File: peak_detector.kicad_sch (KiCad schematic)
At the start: 8 parts, among them U1 AD8001AR, U2 AD8039

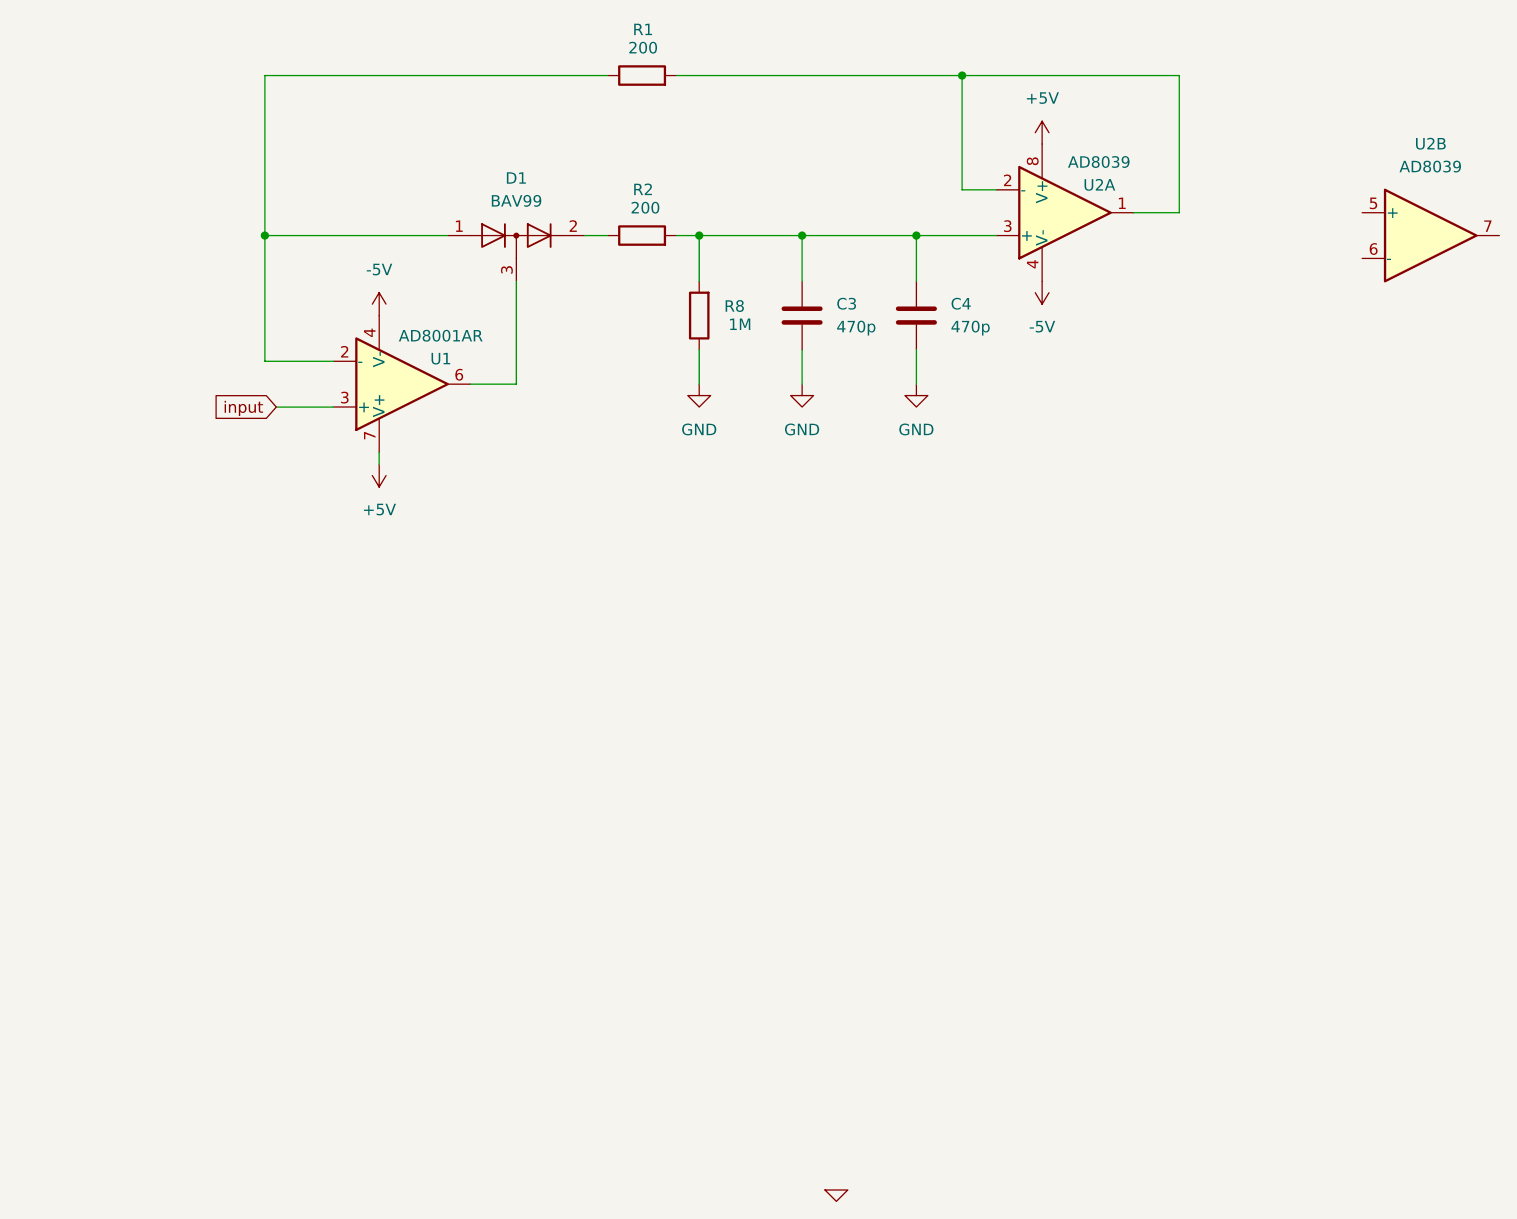
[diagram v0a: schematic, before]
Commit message: Dual bjt and MIC920.
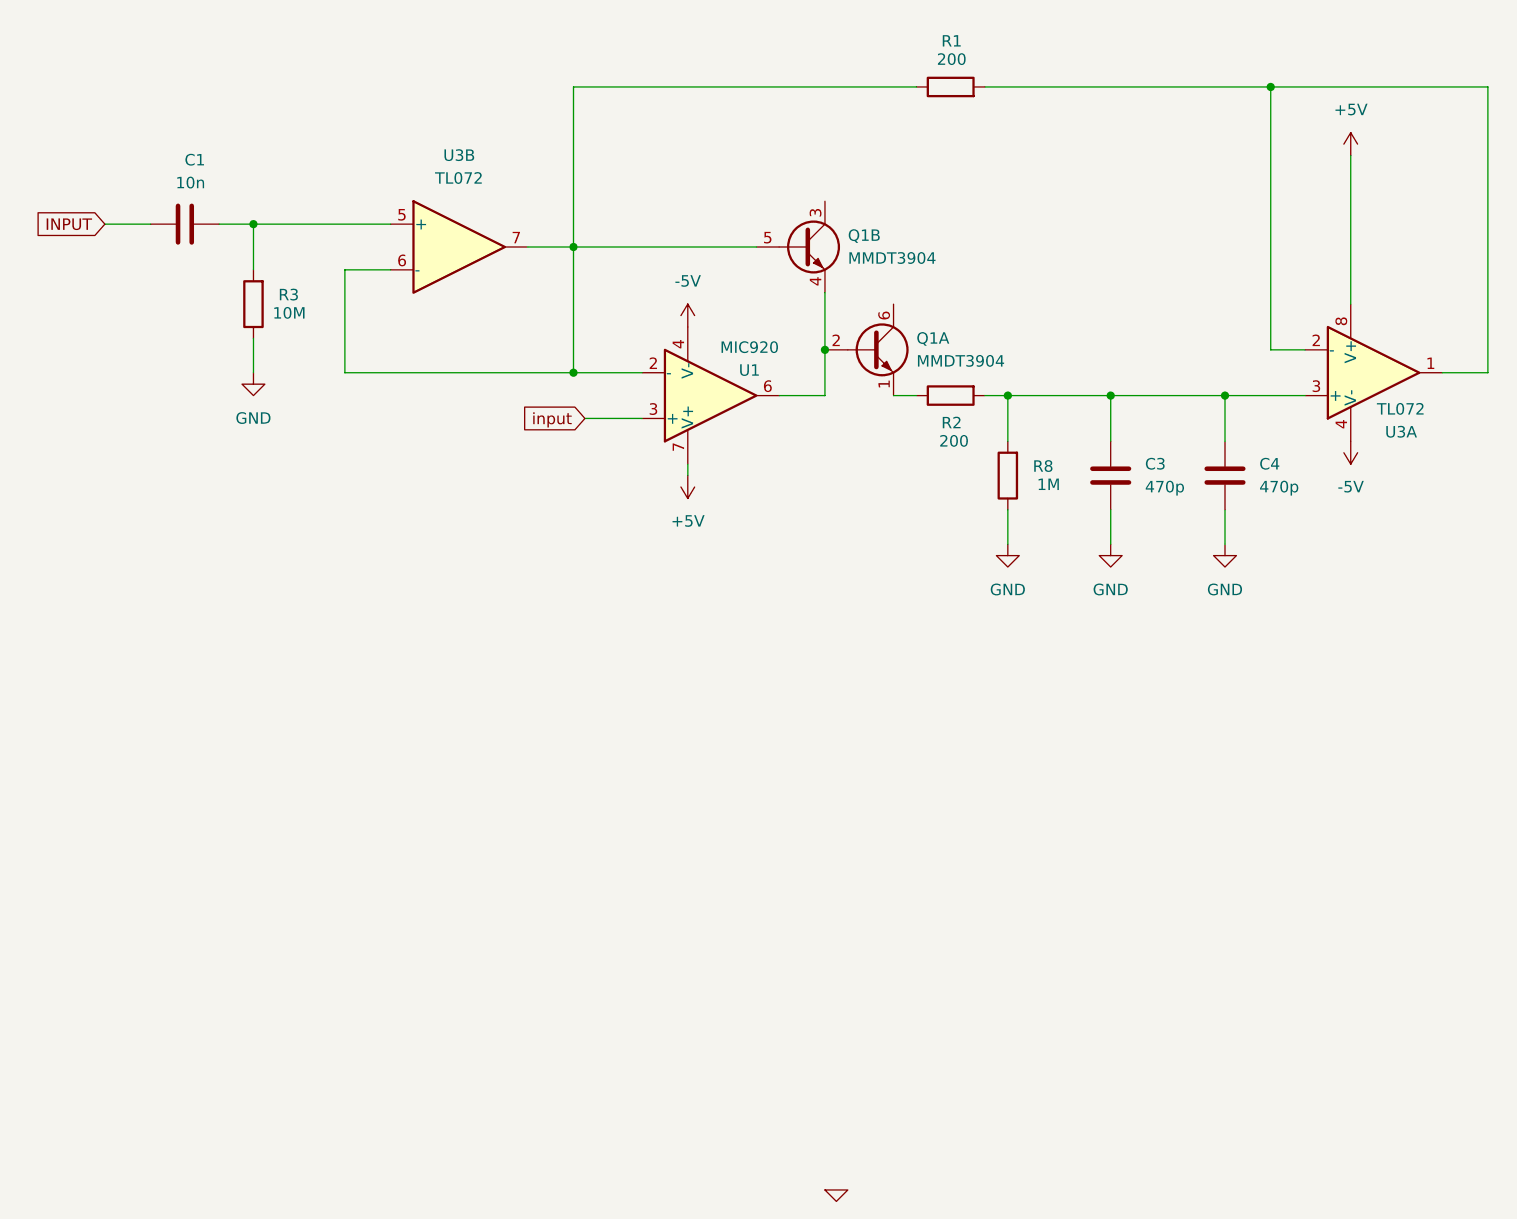
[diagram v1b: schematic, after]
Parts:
- removed D1: BAV99, Package_TO_SOT_SMD:SOT-23, symbol Diode:BAV99
- removed U2: AD8039, Package_SO:SOIC-8_3.9x4.9mm_P1.27mm, symbol Amplifier_Operational:TL072
- added C1: 10n, Capacitor_SMD:C_0603_1608Metric_Pad1.08x0.95mm_HandSolder, symbol Device:C
- added Q1: MMDT3904, Package_TO_SOT_SMD:SOT-363_SC-70-6, symbol Transistor_BJT:MMDT3904
- added R3: 10M, Resistor_SMD:R_0603_1608Metric_Pad0.98x0.95mm_HandSolder, symbol Device:R
- added U3: TL072, Package_SO:SOIC-8_3.9x4.9mm_P1.27mm, symbol Amplifier_Operational:TL072
- U1: value AD8001AR -> MIC920
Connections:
- net +5V: now also U3.8 (V+)
- net -5V: now also U3.4 (V-)
- net GND: now also R3.1
- net at C3.1, C4.1, R2.2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: now also U3.3 (+)
- net at R1.2: now also U3.1, U3.2 (-)
- net at R2.1: now also Q1.1 (E1)
- net at R1.1, U1.2 (-): now also Q1.5 (B2), U3.6 (-), U3.7
- net at U1.6: now also Q1.2 (B1), Q1.4 (E2)
- new net: C1.2, R3.2, U3.5 (+)
- new net INPUT: C1.1
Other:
- moved on the sheet: C3, C4, R1, R2, R8, U1

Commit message: Idk.
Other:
- note added: "add gain on input"
- note added: "add servo"
- note added: "remove"
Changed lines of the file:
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@@
+		)
+	)
+	(text "remove\n"
+		(exclude_from_sim no)
+		(at 183.896 77.978 0)
+		(effects
+			(font
+				(size 1.27 1.27)
+			)
+		)
+	)
+	(text "add servo\n"
+		(exclude_from_sim no)
+		(at 111.252 119.634 0)
+		(effects
+			(font
+				(size 1.27 1.27)
+			)
+		)
+	)
+	(text "add gain on input\n"
+		(exclude_from_sim no)
+		(at 78.486 100.076 0)
+		(effects
+			(font
+				(size 1.27 1.27)
+			)
 		)
 	)
